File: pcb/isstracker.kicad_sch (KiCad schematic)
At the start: 18 parts, among them J1 Display, J2 CONTROL, J3 POWER, J4 Error LED, J5 POWER_OUT, Q2 MMBT2222A, U2 CJT1117-5.0

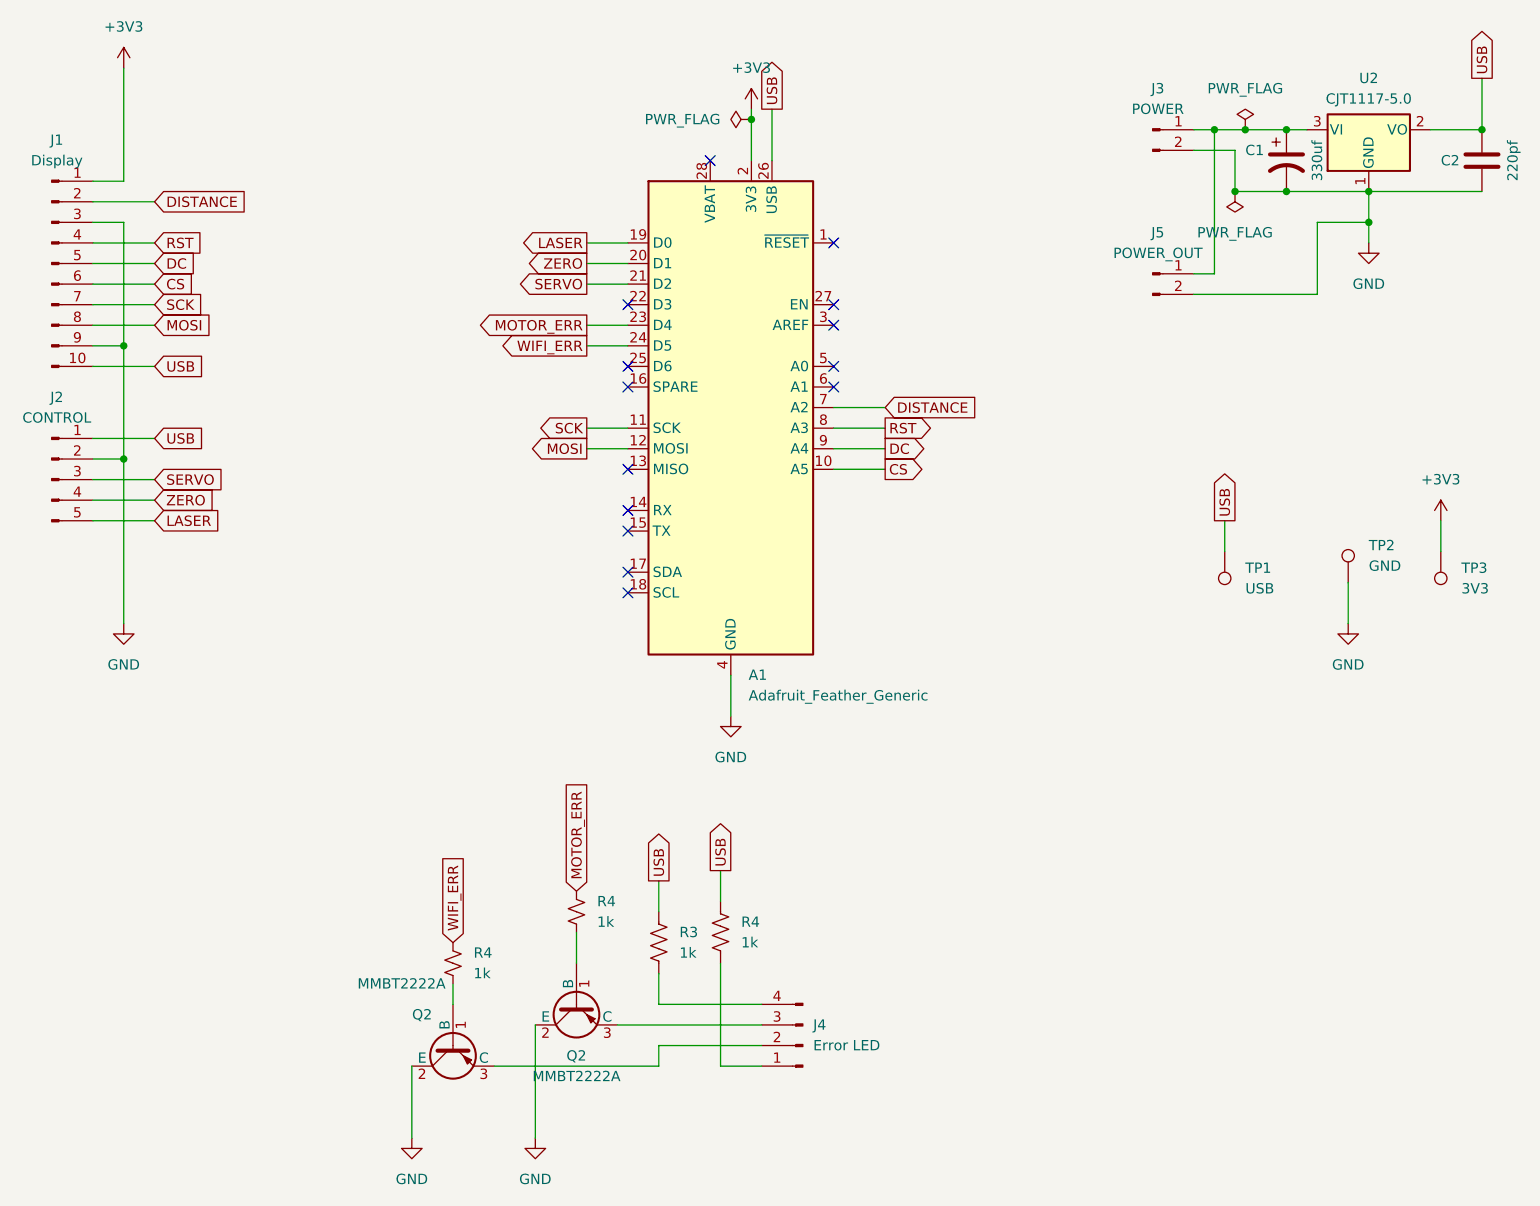
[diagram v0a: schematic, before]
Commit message: Updating to add internal globe LED control
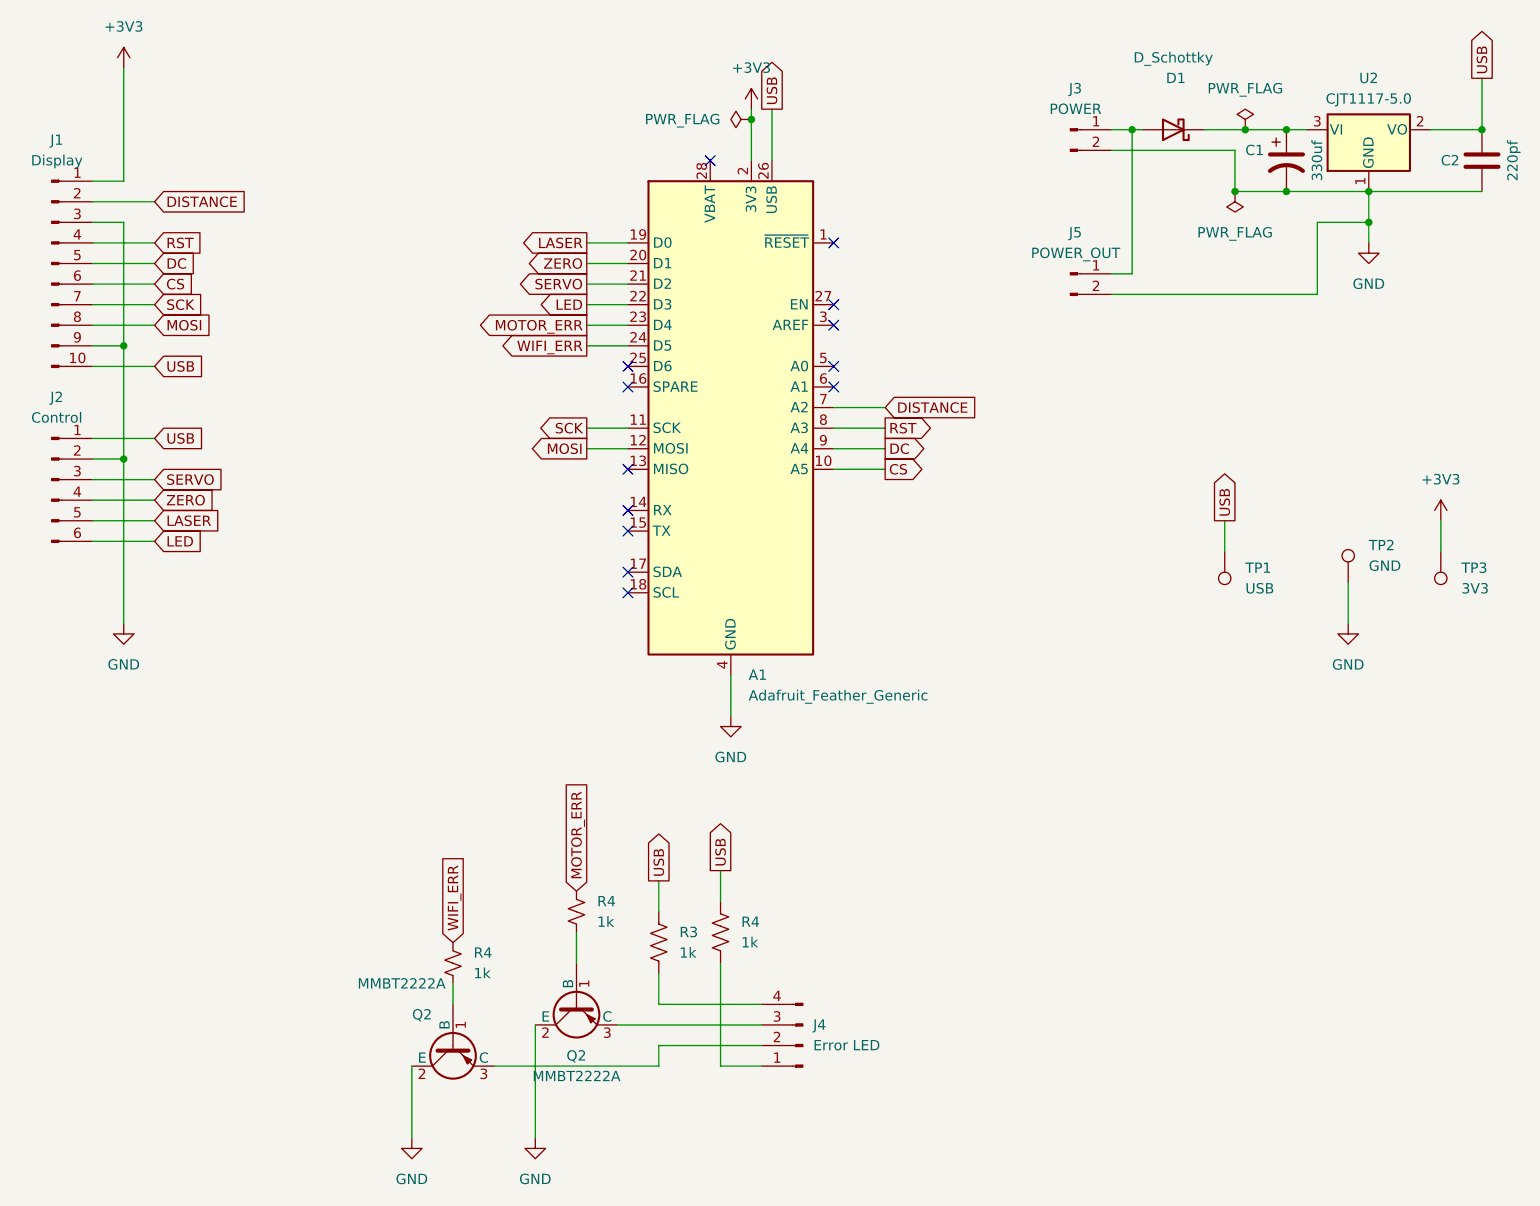
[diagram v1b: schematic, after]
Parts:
- removed J2: CONTROL, Connector_PinHeader_2.54mm:PinHeader_1x05_P2.54mm_Vertical, symbol Connector:Conn_01x05_Pin
- added D1: D_Schottky, Diode_SMD:D_SMA, symbol Device:D_Schottky
- added J2: Control, Connector_PinHeader_2.54mm:PinHeader_1x06_P2.54mm_Vertical, symbol Connector:Conn_01x06_Pin
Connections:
- net GND: now also J2.2 (Pin_2)
- net LASER: now also J2.5 (Pin_5)
- net SERVO: now also J2.3 (Pin_3)
- net USB: now also J2.1 (Pin_1)
- net ZERO: now also J2.4 (Pin_4)
- net at C1.1, U2.3 (VI): now also D1.1 (K); no longer J3.1 (Pin_1), J5.1 (Pin_1)
- net LED: now reaches A1.22 (D3)
- net LED: now also J2.6 (Pin_6)
- new net: D1.2 (A), J3.1 (Pin_1), J5.1 (Pin_1)
- no-connect marks 14 -> 13
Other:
- moved on the sheet: J3, J5
